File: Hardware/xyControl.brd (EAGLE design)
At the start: 160 x 100 mm, 72 parts, among them IC1 ATMEGA2560-16AU, IC2 74HC573D, IC3 K6X4008C1FSMD, IC4 FT232RL, Q7 16M, T1 0-XYTHOBUZ_TASTER

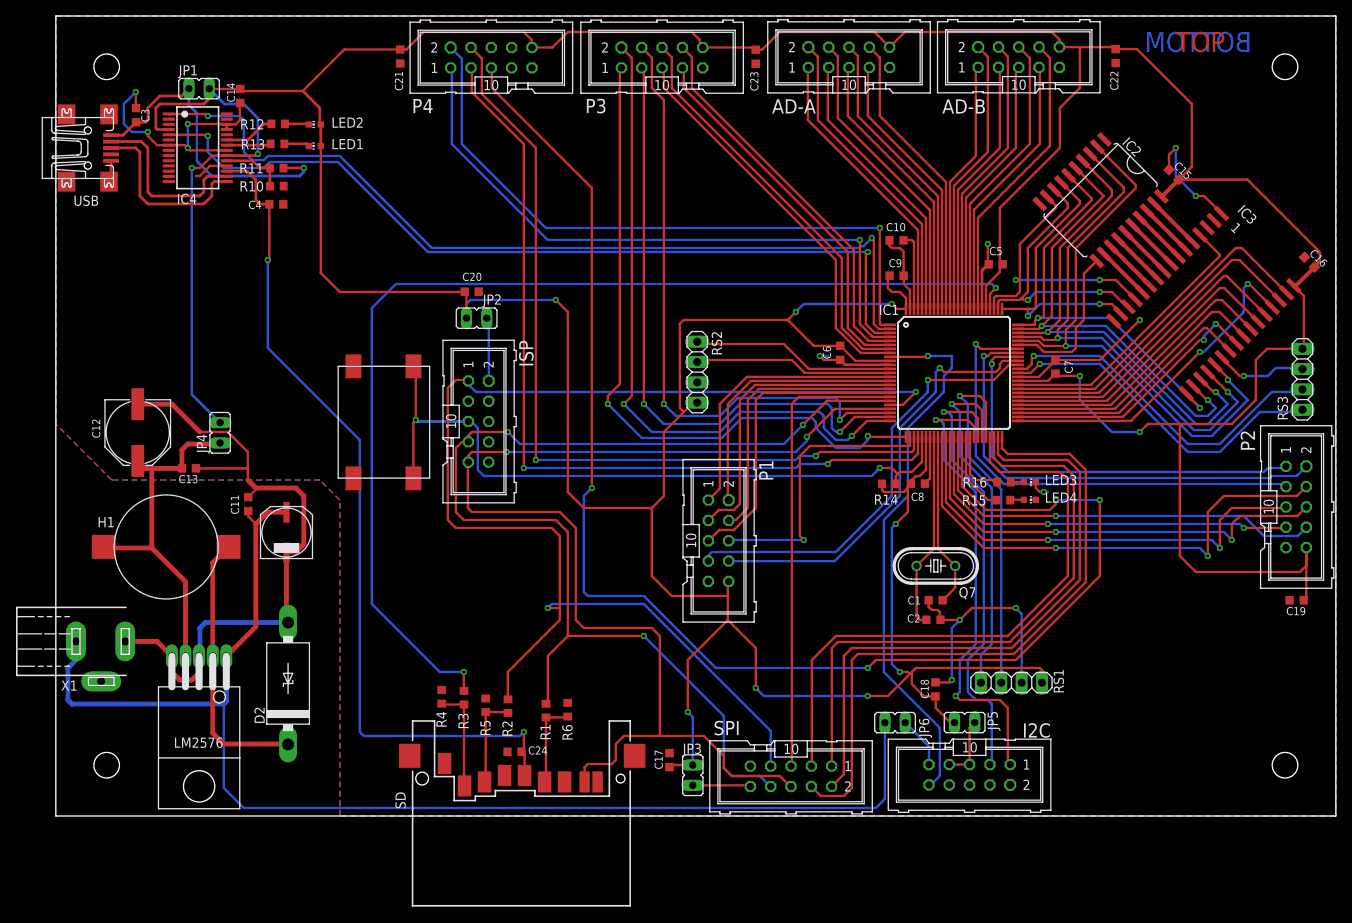
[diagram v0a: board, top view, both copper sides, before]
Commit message: Added bank switching.
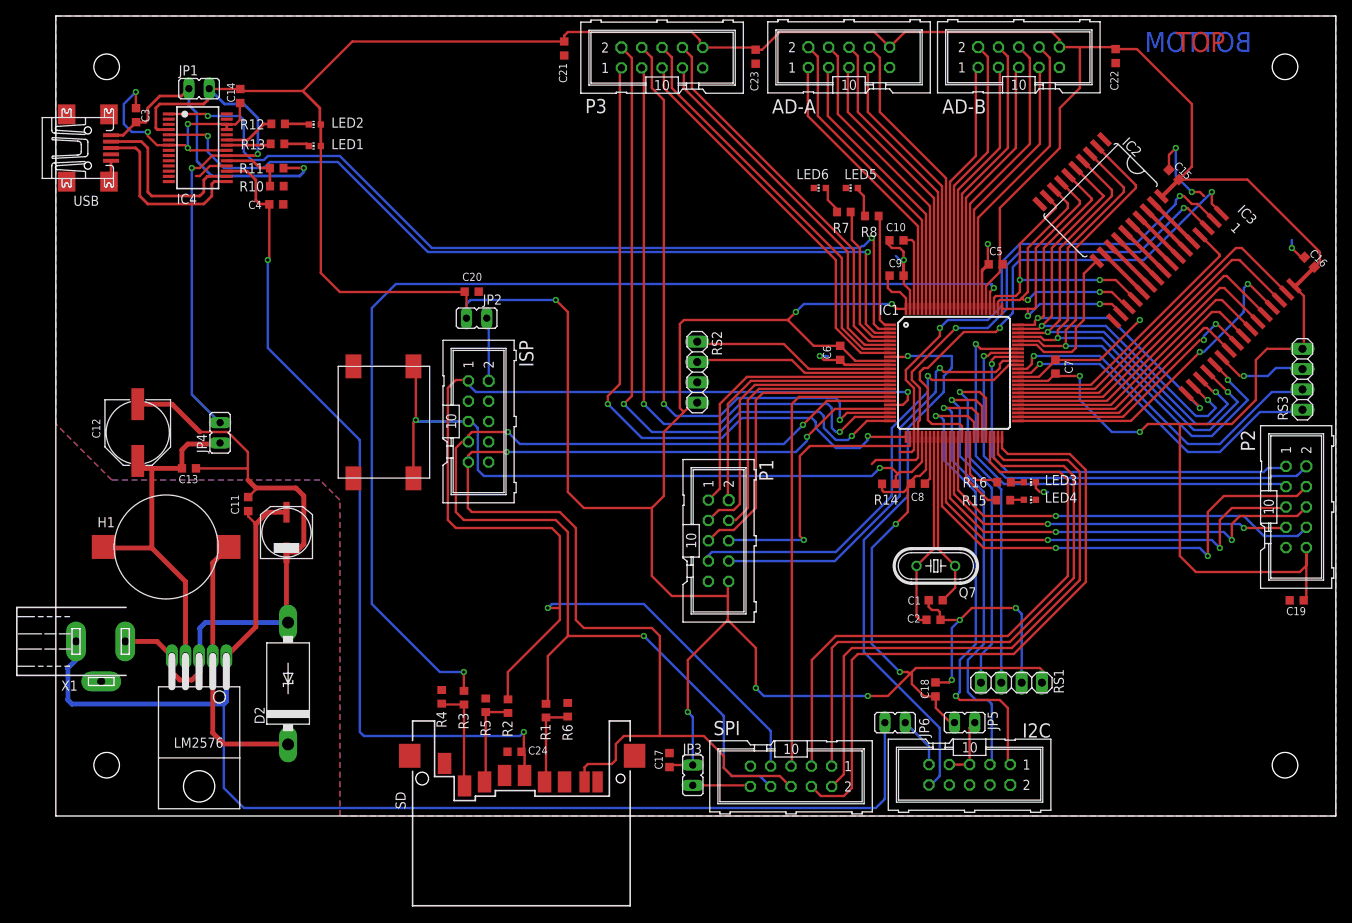
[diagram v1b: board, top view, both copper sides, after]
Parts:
- removed P4: (no value), 01-roboternetz-definitionen:ML10
- added LED5, LED6: (no value), led:CHIP-LED0603
- added R7, R8: 1k, resistor:R0603
- moved C21 20.5 mm to (63.5, 95.9)
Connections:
- new net N$70: LED6.A, R7.1
- new net N$71: LED5.A, R8.1
- net GND: now also LED5.C, LED6.C; no longer IC3.1, IC3.2, IC3.3, P4.9
- net N$109: now also IC3.1; no longer P4.5
- net N$114: now also R8.2; no longer P4.2
- net N$115: now also R7.2; no longer P4.1
- net N$59: now also IC3.2; no longer P4.4
- net N$69: now also IC3.3; no longer P4.3
- net VCC: no longer P4.10
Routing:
- net N$109: track 179.3 -> 64.8 mm, vias 4 -> 2
- net N$114: track 82.6 -> 14.6 mm, vias 1 -> 0
- net N$115: track 80.5 -> 18.9 mm, vias 1 -> 0
- net N$59: track 104.3 -> 65.2 mm
- net N$69: track 104.9 -> 67.0 mm
- net N$71: track 0.00 -> 3.87 mm
- net N$70: track 0.00 -> 3.58 mm
- net GND: track 252.7 -> 255.9 mm, vias 14 -> 16
- net N$44: track 68.5 -> 70.6 mm
- net N$39: track 158.7 -> 157.3 mm
- net N$46: track 44.9 -> 45.9 mm
- net N$45: track 45.9 -> 46.9 mm
- net N$43: track 56.4 -> 57.4 mm
- net N$42: track 58.6 -> 59.6 mm
- net N$1: track 35.6 -> 34.6 mm
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
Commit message: New 3V3 Regulator.
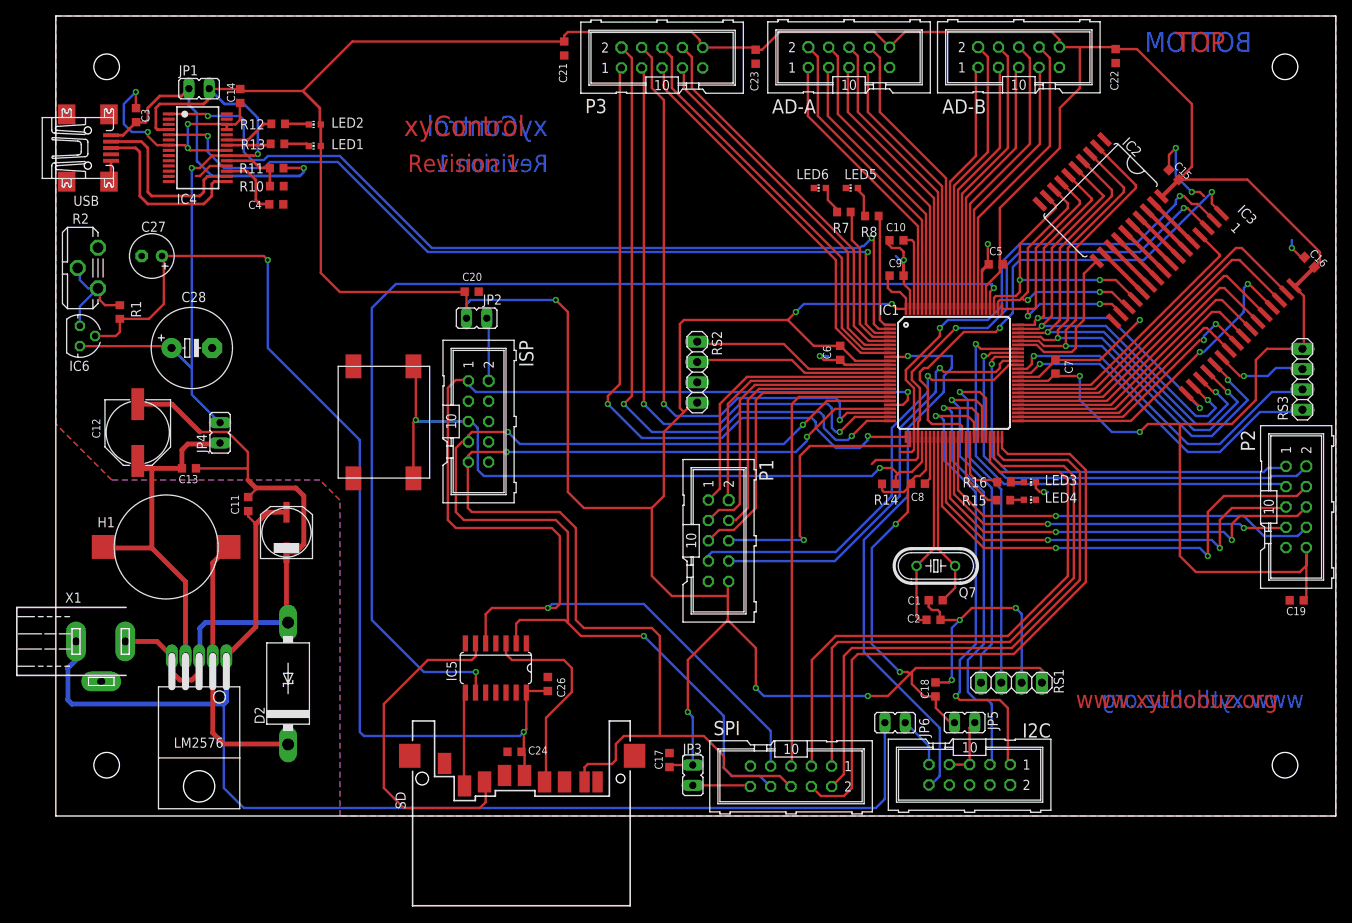
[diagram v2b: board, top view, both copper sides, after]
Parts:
- removed R3: 1k8, resistor:R0603
- removed R4, R5, R6: 3k3, resistor:R0603
- added C26: 100n, resistor:C0603K
- added C27: 1uF, resistor:E2,5-6
- added C28: 330uF, resistor:E5-10,5
- added IC5: 74AHC125, 74xx-eu:SO14
- added IC6: (no value), v-reg:317L
- R1: value 1k8 -> 240
- R2: value 1k8 -> (none); device resistor:R0603 -> LED_Cube:POT_ST10
- moved R2 75.9 mm to (4.00, 68.5), turned to 90 degrees
- moved R1 72.9 mm to (8.00, 63.0)
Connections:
- new net N$73: C4.1, IC4.17
- new net N$83: IC6.1, R1.1, R2.A, R2.S
- net GND: now also C26.1, C27.-, C28.-, IC5.1, IC5.10, IC5.4, IC5.7, R2.E; no longer R4.2, R5.2, R6.2
- net N$37: now also IC5.2; no longer R1.1
- net N$39: now also IC5.5; no longer R2.1
- net N$76: now also IC5.9; no longer R3.1
- net N$77: now also IC5.3; no longer R1.2, R6.1
- net N$78: now also IC5.6; no longer R2.2, R5.1
- net N$79: now also IC5.8; no longer R3.2, R4.1
- net VCC: now also C28.+, IC6.3
- net VDD: now also C26.2, C27.+, IC5.14, IC6.2, R1.2; no longer C4.1, IC4.17
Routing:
- net N$78: track 11.6 -> 43.0 mm
- net VDD: track 105.9 -> 129.2 mm
- net VCC: track 697.9 -> 713.1 mm
- net N$77: track 10.9 -> 25.9 mm
- net N$83: track 0.00 -> 14.3 mm
- net N$73: track 0.00 -> 8.51 mm
- net N$76: track 136.5 -> 139.4 mm
- net N$39: track 157.3 -> 154.6 mm
- net N$37: track 141.1 -> 139.7 mm
- net N$79: track 13.0 -> 11.8 mm
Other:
- board text added: "Revision 1"
- board text added: "www.xythobuz.org"
- board text added: "xyControl"

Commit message: Minor fixes.
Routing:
- net N$69: track 67.0 -> 58.3 mm
- net N$59: track 65.2 -> 61.7 mm
- net VDD: track 129.2 -> 127.8 mm
- net N$37: track 139.7 -> 138.5 mm
- net N$38: track 145.8 -> 144.9 mm
- net N$43: track 57.4 -> 56.5 mm
- net N$5: track 58.3 -> 57.5 mm
- net N$3: track 36.9 -> 36.2 mm
- net N$4: track 52.7 -> 52.1 mm
- net N$39: track 154.6 -> 154.0 mm
- net N$90: track 44.6 -> 45.2 mm
- net N$8: track 72.2 -> 71.7 mm

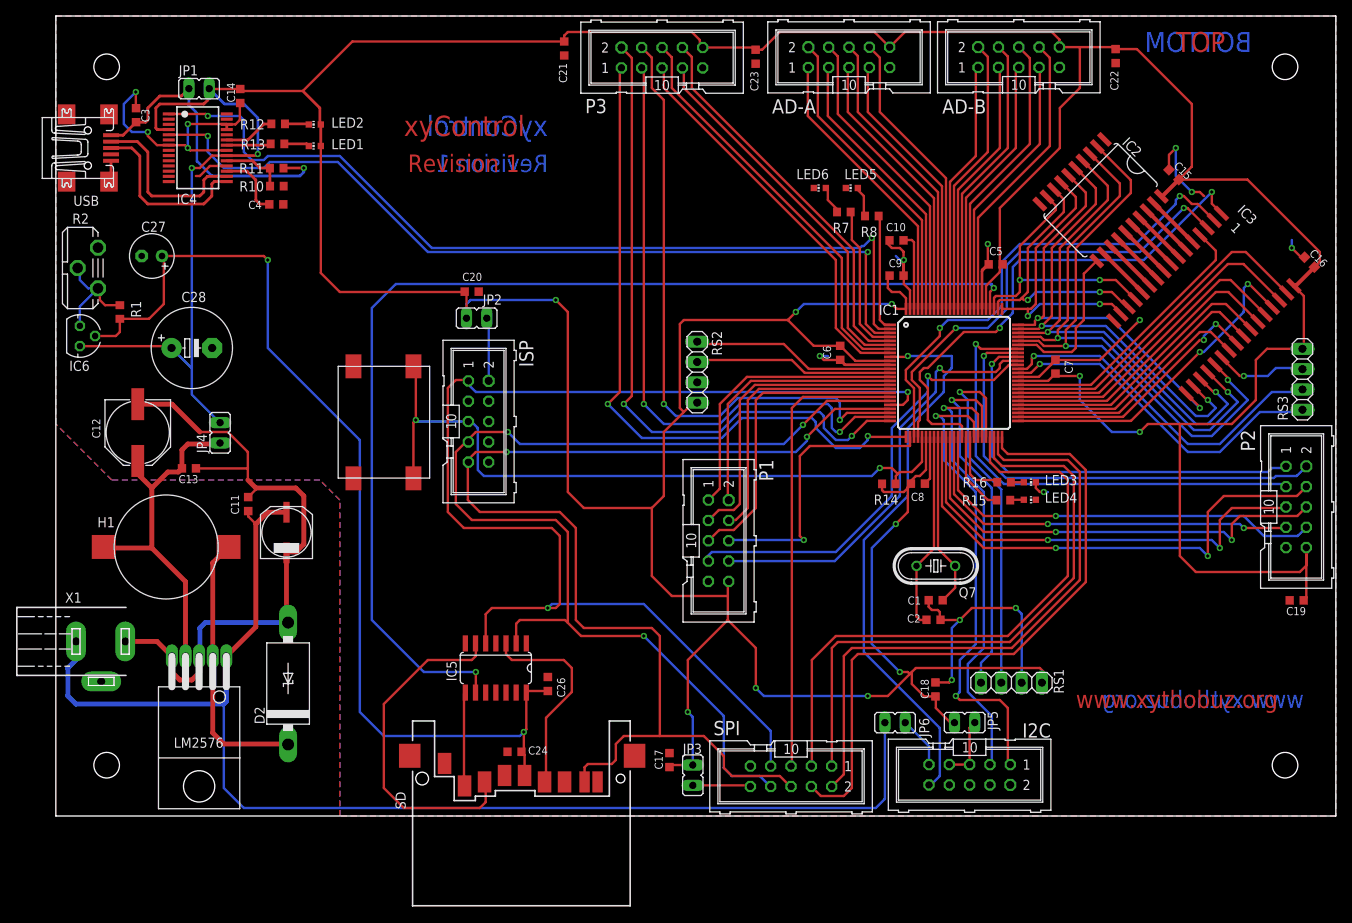
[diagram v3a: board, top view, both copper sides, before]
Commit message: Extended XMEM bank switching.
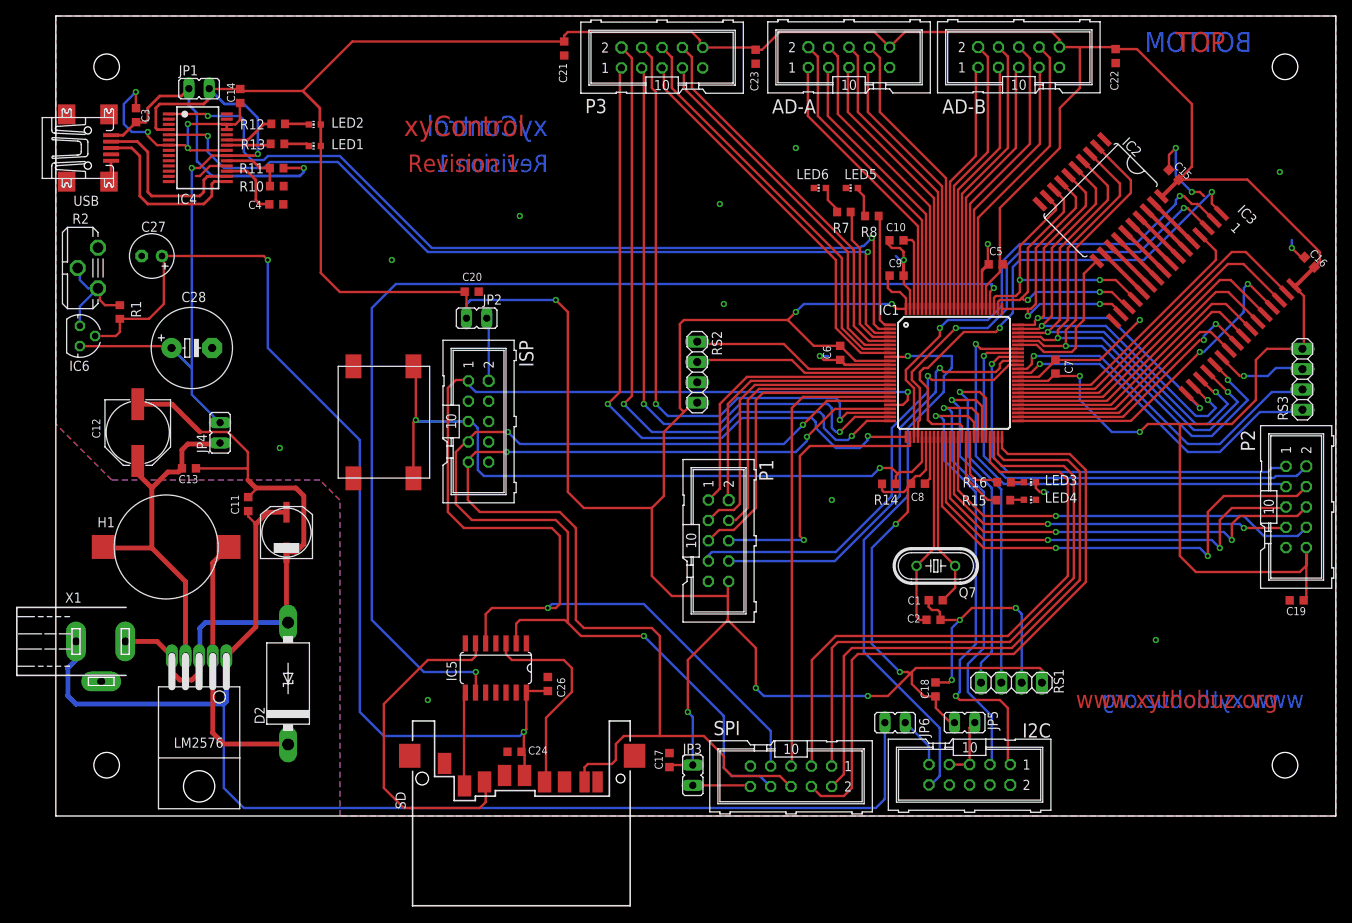
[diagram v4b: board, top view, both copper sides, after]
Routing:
- net N$120: track 78.4 -> 78.9 mm
- net GND: vias 16 -> 26
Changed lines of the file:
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@@
 <contactref element="R2" pad="E"/>
 <contactref element="C27" pad="-"/>
+<via x="97" y="39.5" extent="1-16" drill="0.4" shape="octagon"/>
+<via x="83.5" y="64" extent="1-16" drill="0.4" shape="octagon"/>
+<via x="83" y="76.5" extent="1-16" drill="0.4" shape="octagon"/>
+<via x="137.5" y="22" extent="1-16" drill="0.4" shape="octagon"/>
+<via x="153" y="80.5" extent="1-16" drill="0.4" shape="octagon"/>
+<via x="92.5" y="83.5" extent="1-16" drill="0.4" shape="octagon"/>
+<via x="58" y="75" extent="1-16" drill="0.4" shape="octagon"/>
+<via x="42" y="69.5" extent="1-16" drill="0.4" shape="octagon"/>
+<via x="46.5" y="14.5" extent="1-16" drill="0.4" shape="octagon"/>
+<via x="28" y="46" extent="1-16" drill="0.4" shape="octagon"/>
 </signal>
 <signal name="VCC">
@@
 <wire x1="97.5" y1="52.25" x2="85.25" y2="52.25" width="0.3" layer="16"/>
 <wire x1="85.25" y1="52.25" x2="83" y2="50" width="0.3" layer="16"/>
-<wire x1="83" y1="50" x2="77.5" y2="50" width="0.3" layer="16"/>
-<wire x1="77.5" y1="50" x2="76" y2="51.5" width="0.3" layer="16"/>
-<via x="76" y="51.5" extent="1-16" drill="0.4" shape="octagon"/>
-<wire x1="76" y1="51.5" x2="76" y2="89.5" width="0.3" layer="1"/>
-<wire x1="76" y1="89.5" x2="74.5" y2="91" width="0.3" layer="1"/>
+<wire x1="83" y1="50" x2="76.5" y2="50" width="0.3" layer="16"/>
+<wire x1="76.5" y1="50" x2="75" y2="51.5" width="0.3" layer="16"/>
+<via x="75" y="51.5" extent="1-16" drill="0.4" shape="octagon"/>
+<wire x1="75" y1="51.5" x2="75" y2="90.5" width="0.3" layer="1"/>
+<wire x1="75" y1="90.5" x2="74.5" y2="91" width="0.3" layer="1"/>
 <wire x1="74.5" y1="91" x2="74.5" y2="94.8" width="0.3" layer="1"/>
 <wire x1="74.5" y1="94.8" x2="73.24" y2="96.06" width="0.3" layer="1"/>
